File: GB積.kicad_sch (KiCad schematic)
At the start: 16 parts, among them U1 ${SIM.PARAMS}, U2 ${SIM.PARAMS}, U3 ${SIM.PARAMS}

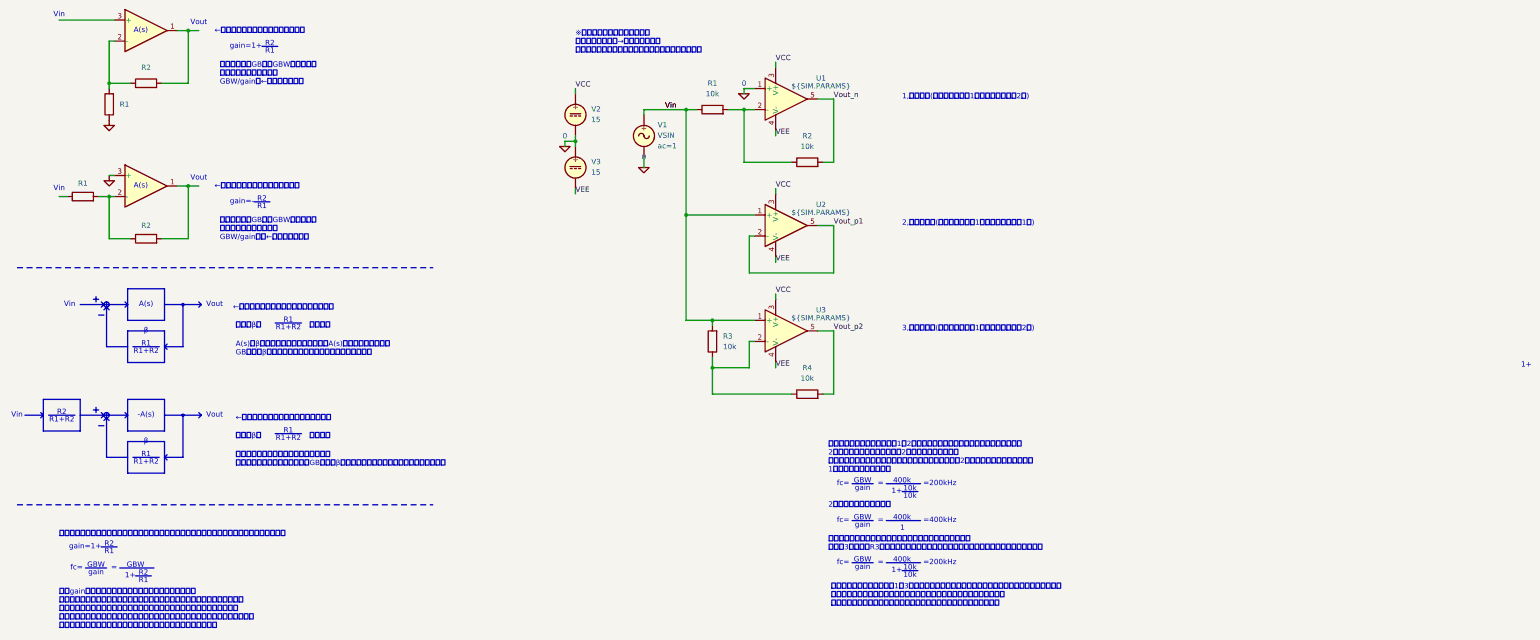
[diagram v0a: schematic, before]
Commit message: レイアウトの修正
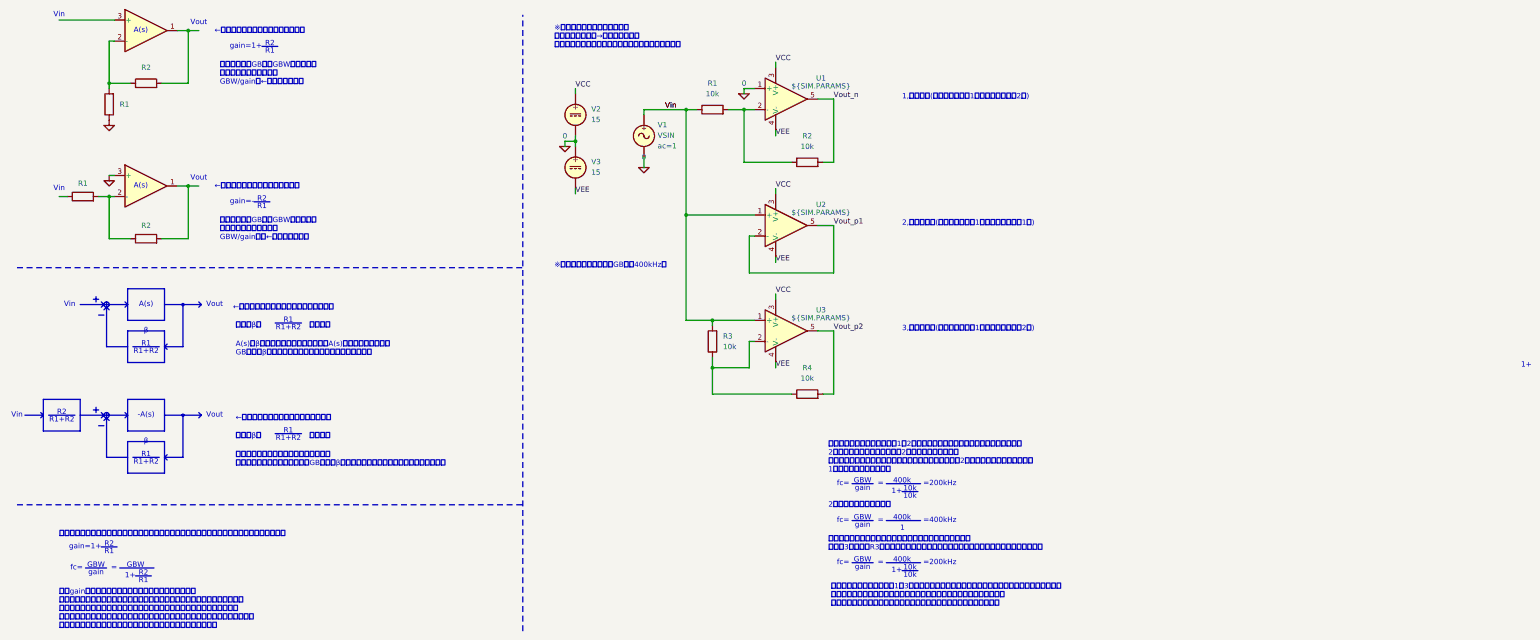
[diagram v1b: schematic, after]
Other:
- note added: "※これらのオペアンプのGB積は400kHz。"
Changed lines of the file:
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@@
 	(polyline
 		(pts
-			(xy 17.78 133.35) (xy 118.11 133.35)
+			(xy 17.78 133.35) (xy 139.7 133.35)
 		)
 		(stroke
@@
 		)
 	)
+	(polyline
+		(pts
+			(xy 139.7 163.83) (xy 139.7 15.24)
+		)
+		(stroke
+			(width 0.2)
+			(type dash)
+		)
+	)
 	(wire
 		(pts
@@
 	(polyline
 		(pts
-			(xy 17.78 76.2) (xy 118.11 76.2)
+			(xy 17.78 76.2) (xy 139.7 76.2)
 		)
 		(stroke
@@
 		)
 	)
+	(text "※これらのオペアンプのGB積は400kHz。"
+		(exclude_from_sim no)
+		(at 147.32 74.93 0)
+		(effects
+			(font
+				(size 1.27 1.27)
+			)
+			(justify left top)
+		)
+	)
 	(text "シミュレーションを行うと、1と2の回路では直流利得が等しいのにかかわらず、\n2の回路のほうが遮断周波数が2倍高いことが分かる。\nこれは、シグナルゲインが等しいもののノイズゲインが2倍異なっているからである。\n1の回路の遮断周波数は、"
 		(exclude_from_sim no)
@@
 	(text "※シミュレーションの実行方法\n上部タブの、検査→シミュレーター\nでシミュレーター起動。その後、実行ボタンを押す。"
 		(exclude_from_sim no)
-		(at 152.4 19.05 0)
-		(effects
-			(font
+		(at 147.32 17.78 0)
+		(effects
+			(font

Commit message: 軽微な修正
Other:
- note added: "このgain(βの逆数)は、所謂ノイズゲインと呼ばれるものである。 ノイズゲインは、オペアンプ内部で発生する雑音が、すべて非反転入力端子で 発生したものとモデル化したとき、その雑音に対するゲインと定義される。 オペアンプ回路の周波数特性を考えるときは、シグナルに対するゲインではなく、 ノイズゲインを用いるのが正しい。位相余裕を考えるときも同様。"
- note removed: "このgainは、所謂ノイズゲインと呼ばれるものである。 ノイズゲインは、オペアンプ内部で発生する雑音が、すべて非反転入力端子で 発生したものとモデル化したとき、その雑音に対するゲインと定義される。 オペアンプ回路の周波数特性を考えるときは、シグナルに対するゲインではなく、 ノイズゲインを用いるのが正しい。位相余裕を考えるときも同様。"
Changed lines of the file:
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@@
 		)
 	)
-	(text "このgainは、所謂ノイズゲインと呼ばれるものである。\nノイズゲインは、オペアンプ内部で発生する雑音が、すべて非反転入力端子で\n発生したものとモデル化したとき、その雑音に対するゲインと定義される。\nオペアンプ回路の周波数特性を考えるときは、シグナルに対するゲインではなく、\nノイズゲインを用いるのが正しい。位相余裕を考えるときも同様。"
+	(text "このgain(βの逆数)は、所謂ノイズゲインと呼ばれるものである。\nノイズゲインは、オペアンプ内部で発生する雑音が、すべて非反転入力端子で\n発生したものとモデル化したとき、その雑音に対するゲインと定義される。\nオペアンプ回路の周波数特性を考えるときは、シグナルに対するゲインではなく、\nノイズゲインを用いるのが正しい。位相余裕を考えるときも同様。"
 		(exclude_from_sim no)
 		(at 27.94 153.67 0)

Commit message: 軽微な修正
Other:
- note added: "1/β"
- note added: "1/β=1+"
- note added: "NG"
- note added: "|gain|"
- note added: "←これは正しい"
- note added: "←これは間違い！"
- note added: "このβの逆数は、所謂ノイズゲイン(NG)と呼ばれるものである。 ノイズゲインは、オペアンプ内部で発生する雑音が、すべて非反転入力端子で 発生したものとモデル化したとき、その雑音に対するゲインと定義される。 オペアンプ回路の周波数特性を考えるときは、シグナルに対するゲインではなく、 ノイズゲインを用いるのが正しい。位相余裕を考えるときも同様。"
- note added: "と計算される。これは回路1と3のシミュレーション結果が完全に一致することを説明している。 これらのことから、ノイズゲインとシグナルゲインを別に設定することで 直流利得を保ったまま周波数特性を変えることができることが分かる。 応用として、シングルエンド→差動変換をする回路で、差動の上下を同じ周波数特性にすることが可能。"
- note added: "オペアンプのGB積をGBWとすると、 この回路の遮断周波数は"
- note removed: "gain"
- note removed: "このgain(βの逆数)は、所謂ノイズゲインと呼ばれるものである。 ノイズゲインは、オペアンプ内部で発生する雑音が、すべて非反転入力端子で 発生したものとモデル化したとき、その雑音に対するゲインと定義される。 オペアンプ回路の周波数特性を考えるときは、シグナルに対するゲインではなく、 ノイズゲインを用いるのが正しい。位相余裕を考えるときも同様。"
- note removed: "と計算される。これは回路1と3のシミュレーション結果が完全に一致することを説明している。 これらのことから、ノイズゲインとシグナルゲインを別に設定することで 直流利得を保ったまま周波数特性を変えることができることが分かる。"
- note removed: "オペアンプのGB積をGBWとすると、 この回路の遮断周波数は GBW/gain ←これは正しい。"
- note removed: "オペアンプのGB積をGBWとすると、 この回路の遮断周波数は GBW/gain ←これは間違い！"

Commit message: 表現の修正
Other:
- note added: "このβの逆数は、所謂ノイズゲイン(NG)と呼ばれるものである。 ノイズゲインは、オペアンプ内部で発生する雑音が、すべて非反転入力端子で 発生したものとモデル化したとき、その雑音に対するゲインと定義される。 オペアンプ回路の周波数特性を考えるときは、シグナルに対するゲインではなく、 ノイズゲインを用いるのが正しい。出力オフセット電圧を考えるときもノイズゲインを用いる。"
- note added: "と求まり、これはシミュレーションの結果と一致している。 また、3の回路のR3は、仮想接地を考えると一見意味のない抵抗に見えるがノイズゲインに関わっており、"
- note added: "と計算される。これは回路1と3のシミュレーション結果が完全に一致することを説明している。 これらのことから、ノイズゲインとシグナルゲインを別に設定することで 直流利得を保ったまま周波数特性を変えることができることが分かる。 応用として、シングルエンド→差動変換をする回路で、差動ペアの周波数特性をそろえるなどができる。"
- note removed: "-A(s)"
- note removed: "β"
- note removed: "このβの逆数は、所謂ノイズゲイン(NG)と呼ばれるものである。 ノイズゲインは、オペアンプ内部で発生する雑音が、すべて非反転入力端子で 発生したものとモデル化したとき、その雑音に対するゲインと定義される。 オペアンプ回路の周波数特性を考えるときは、シグナルに対するゲインではなく、 ノイズゲインを用いるのが正しい。位相余裕を考えるときも同様。"
- note removed: "と求まり、これはシミュレーションの結果と一致している。 また、3の回路のR3は、一見意味のない抵抗に見えるが、ノイズゲインに関わっており、"
- note removed: "と計算される。これは回路1と3のシミュレーション結果が完全に一致することを説明している。 これらのことから、ノイズゲインとシグナルゲインを別に設定することで 直流利得を保ったまま周波数特性を変えることができることが分かる。 応用として、シングルエンド→差動変換をする回路で、差動の上下を同じ周波数特性にすることが可能。"
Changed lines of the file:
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@@
 	(polyline
 		(pts
-			(xy 19.685 111.76) (xy 24.13 111.76)
+			(xy 19.685 111.76) (xy 24.765 111.76)
 		)
 		(stroke
@@
 	(polyline
 		(pts
-			(xy 39.37 84.455) (xy 39.37 85.725)
-		)
-		(stroke
-			(width 0)
-			(type default)
-		)
-	)
-	(polyline
-		(pts
 			(xy 43.815 112.395) (xy 44.45 111.76)
 		)
@@
 		(pts
 			(xy 59.055 31.75) (xy 59.055 19.05)
+		)
+		(stroke
+			(width 0)
+			(type default)
+		)
+	)
+	(polyline
+		(pts
+			(xy 25.4 111.76) (xy 26.67 111.76)
 		)
 		(stroke
@@
 	(polyline
 		(pts
-			(xy 23.495 112.395) (xy 24.13 111.76)
+			(xy 24.13 112.395) (xy 24.765 111.76)
 		)
 		(stroke
@@
 		(pts
 			(xy 38.1 85.725) (xy 38.735 85.09)
-		)
-		(stroke
-			(width 0)
-			(type default)
-		)
-	)
-	(polyline
-		(pts
-			(xy 38.735 111.76) (xy 40.005 111.76)
 		)
 		(stroke
@@
 	(polyline
 		(pts
-			(xy 33.02 111.76) (xy 38.735 111.76)
+			(xy 34.925 111.76) (xy 38.735 111.76)
 		)
 		(stroke
@@
 	(polyline
 		(pts
-			(xy 25.4 111.76) (xy 31.75 111.76)
+			(xy 27.305 111.76) (xy 33.655 111.76)
 		)
 		(stroke
@@
 		)
 	)
-	(polyline
-		(pts
-			(xy 39.37 111.125) (xy 39.37 112.395)
-		)
-		(stroke
-			(width 0)
-			(type default)
-		)
-	)
 	(wire
 		(pts
@@
 	(polyline
 		(pts
-			(xy 23.495 111.125) (xy 24.13 111.76)
+			(xy 24.13 111.125) (xy 24.765 111.76)
 		)
 		(stroke
@@
 	(polyline
 		(pts
-			(xy 38.735 85.09) (xy 40.005 85.09)
-		)
-		(stroke
-			(width 0)
-			(type default)
-		)
-	)
-	(polyline
-		(pts
 			(xy 53.34 95.25) (xy 53.975 94.615)
 		)
@@
 	)
 	(rectangle
-		(start 24.13 107.95)
-		(end 33.02 115.57)
+		(start 24.765 107.95)
+		(end 34.925 115.57)
 		(stroke
 			(width 0)
@@
 		)
 	)
-	(text "β"
-		(exclude_from_sim no)
-		(at 48.895 118.11 0)
-		(effects
-			(font
-				(size 1.27 1.27)
-			)
-		)
-	)
 	(text "R1+R2"
 		(exclude_from_sim no)
-		(at 28.575 113.665 0)
+		(at 30.48 113.665 0)
 		(effects
 			(font
@@
 		)
 	)
-	(text "β"
-		(exclude_from_sim no)
-		(at 48.895 91.44 0)
-		(effects
-			(font
-				(size 1.27 1.27)
-			)
-		)
-	)
 	(text "Vout"
 		(exclude_from_sim no)
@@
 		)
 	)
-	(text "と計算される。これは回路1と3のシミュレーション結果が完全に一致することを説明している。\nこれらのことから、ノイズゲインとシグナルゲインを別に設定することで\n直流利得を保ったまま周波数特性を変えることができることが分かる。\n応用として、シングルエンド→差動変換をする回路で、差動の上下を同じ周波数特性にすることが可能。"
+	(text "と計算される。これは回路1と3のシミュレーション結果が完全に一致することを説明している。\nこれらのことから、ノイズゲインとシグナルゲインを別に設定することで\n直流利得を保ったまま周波数特性を変えることができることが分かる。\n応用として、シングルエンド→差動変換をする回路で、差動ペアの周波数特性をそろえるなどができる。"
 		(exclude_from_sim no)
 		(at 210.185 151.765 0)
@@
 		)
 	)
-	(text "と求まり、これはシミュレーションの結果と一致している。\nまた、3の回路のR3は、一見意味のない抵抗に見えるが、ノイズゲインに関わっており、"
+	(text "と求まり、これはシミュレーションの結果と一致している。\nまた、3の回路のR3は、仮想接地を考えると一見意味のない抵抗に見えるがノイズゲインに関わっており、"
 		(exclude_from_sim no)
 		(at 209.55 140.335 0)
@@
 	(text "R2"
 		(exclude_from_sim no)
-		(at 28.575 111.125 0)
+		(at 30.48 111.125 0)
 		(effects
 			(font
@@
 		)
 	)
-	(text "このβの逆数は、所謂ノイズゲイン(NG)と呼ばれるものである。\nノイズゲインは、オペアンプ内部で発生する雑音が、すべて非反転入力端子で\n発生したものとモデル化したとき、その雑音に対するゲインと定義される。\nオペアンプ回路の周波数特性を考えるときは、シグナルに対するゲインではなく、\nノイズゲインを用いるのが正しい。位相余裕を考えるときも同様。"
+	(text "このβの逆数は、所謂ノイズゲイン(NG)と呼ばれるものである。\nノイズゲインは、オペアンプ内部で発生する雑音が、すべて非反転入力端子で\n発生したものとモデル化したとき、その雑音に対するゲインと定義される。\nオペアンプ回路の周波数特性を考えるときは、シグナルに対するゲインではなく、\nノイズゲインを用いるのが正しい。出力オフセット電圧を考えるときもノイズゲインを用いる。\n"
 		(exclude_from_sim no)
 		(at 27.94 153.67 0)
@@
 		)
 	)
-	(text "-A(s)"
+	(text "A(s)"
 		(exclude_from_sim no)
 		(at 48.895 111.76 0)
